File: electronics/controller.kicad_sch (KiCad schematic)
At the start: 86 parts, among them J1 Power_Supply_Connector, J10 Heated_Bed_Thermistor_Connect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, J11 Bl_Touch_Gnd_ZMin_Connector, J12 Bl_Touch_Signal_Vcc_Gnd_Conne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, J13 Motor_A_Connector, J14 Motor_B_Connector, J15 Motor_Z_Connector, J16 Motor_E_Connector, J2 X_Axis_Endstop_Connector, J3 Y_Axis_Endstop_Connector, J4 USB_C_Receptacle_USB2.0, J5 Hotend_Connector, J6 Heated_Bed_Connector, J7 Hotend_Fan_Connector, J8 Layer_Fan_Connector, J9 Hotend_Thermistor_Connector, Q1 PSMN4R1-30YLC, Q2 PSMN4R1-30YLC, Q3 PSMN4R1-30YLC, Q4 PSMN4R1-30YLC, SW1 EN_Button, SW2 Boot_Button, SW3 Pause/Resume_Button, U1 AZ1084CD-3.3TRG1, U10 MCU45P04-TP, U11 K7805MT-1000R4, U3 ESP32-S3-WROOM-1, U4 MT29F2G01ABAGDWB-IT, U5 USBLC6-2SC6, U6 TMC2209_SILENTSTEPSTICK, U7 TMC2209_SILENTSTEPSTICK, U8 TMC2209_SILENTSTEPSTICK, U9 TMC2209_SILENTSTEPSTICK

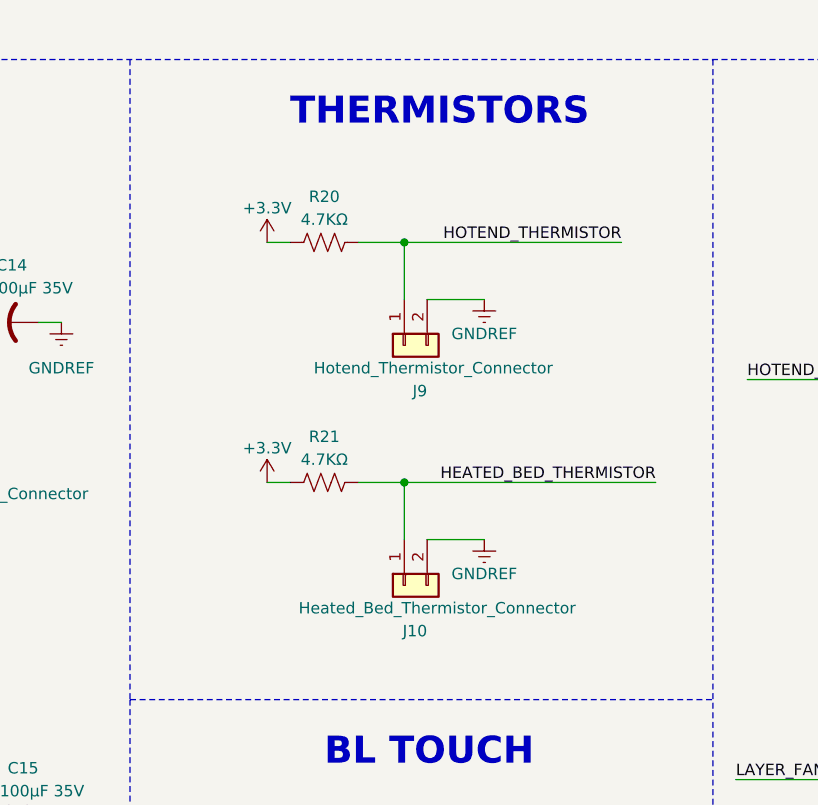
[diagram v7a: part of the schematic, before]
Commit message: ⚡️ Add EMI filters on thermistors on KiCad schematic
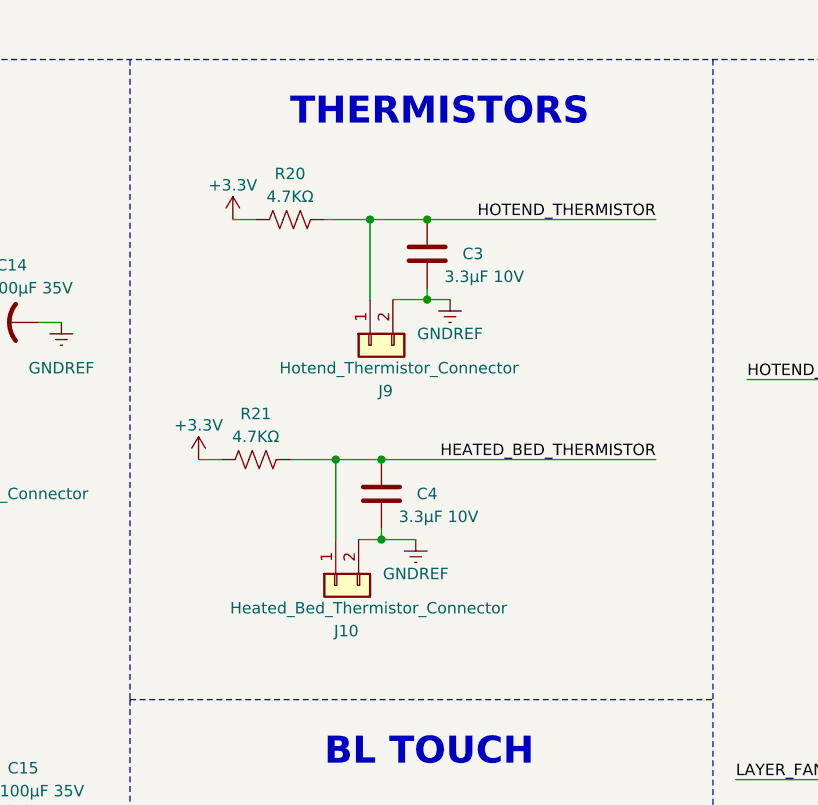
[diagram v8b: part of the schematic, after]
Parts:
- added C3, C4: 3.3µF 10V, symbol Project:C
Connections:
- net GNDREF: now also C3.1, C4.1
- net HEATED_BED_THERMISTOR: now also C4.2
- net HOTEND_THERMISTOR: now also C3.2
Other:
- moved on the sheet: J10, J9, R20, R21
